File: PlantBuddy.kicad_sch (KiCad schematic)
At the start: 72 parts, among them J1 USB_C_Receptacle_USB2.0, J101 JST, J102 J-Link SWD, J4 External, SW1 SW_Push, U1 LTR-303ALS-01, U101 ME6231C33M5G, U102 nRF52832-QFAA, U104 XB5350A, U105 CN809T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

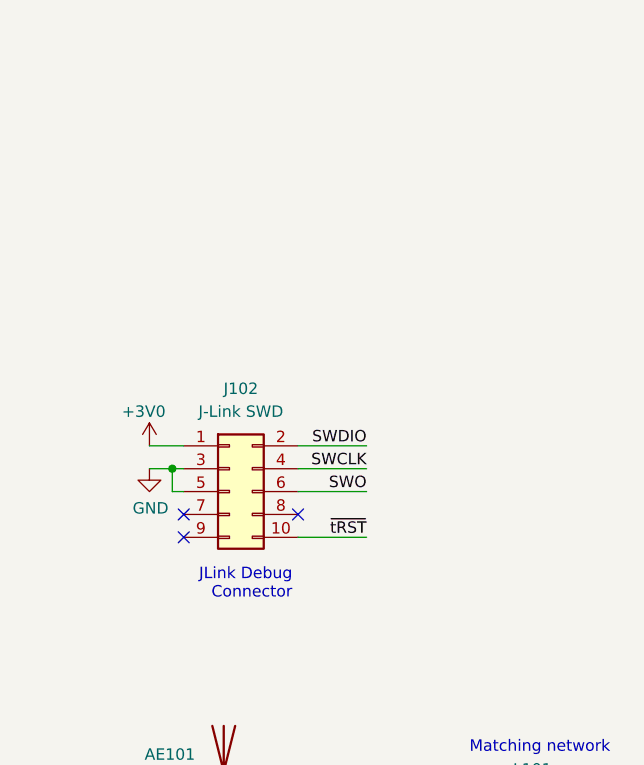
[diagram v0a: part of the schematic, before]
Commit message: Exchanged debug connector for Tag-Connect TC2030-CTX-NL
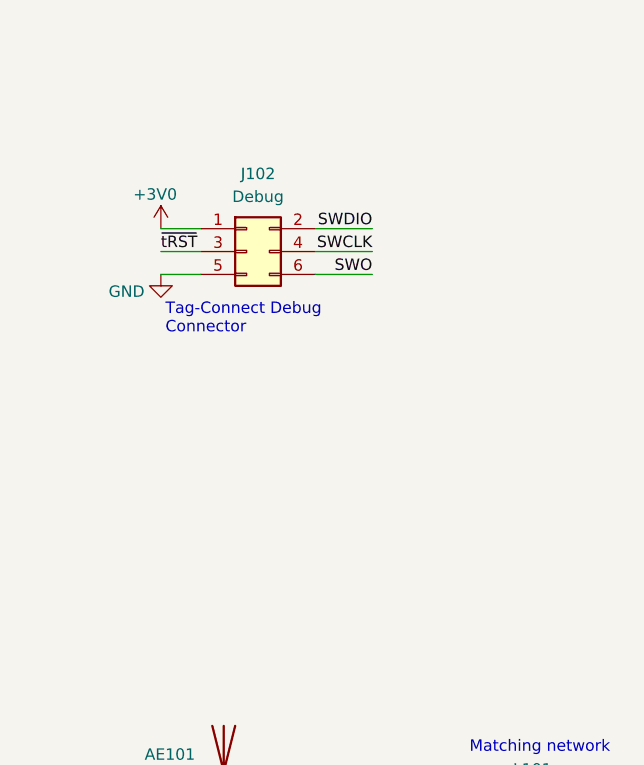
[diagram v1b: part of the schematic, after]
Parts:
- removed J102: J-Link SWD, Connector_PinHeader_1.27mm:PinHeader_2x05_P1.27mm_Vertical, symbol Connector_Generic:Conn_02x05_Odd_Even
- added J102: Debug, Connector:Tag-Connect_TC2030-IDC-NL_2x03_P1.27mm_Vertical, symbol Connector_Generic:Conn_02x03_Odd_Even
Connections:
- net +3V0: now also J102.1 (Pin_1)
- net GND: now also J102.5 (Pin_5)
- net SWCLK: now also J102.4 (Pin_4)
- net SWDIO: now also J102.2 (Pin_2)
- net SWO: now also J102.6 (Pin_6)
- net ~{tRST}: now also J102.3 (Pin_3)
- no-connect marks 26 -> 23
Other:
- note added: "Tag-Connect Debug Connector"
- note removed: "JLink Debug Connector"

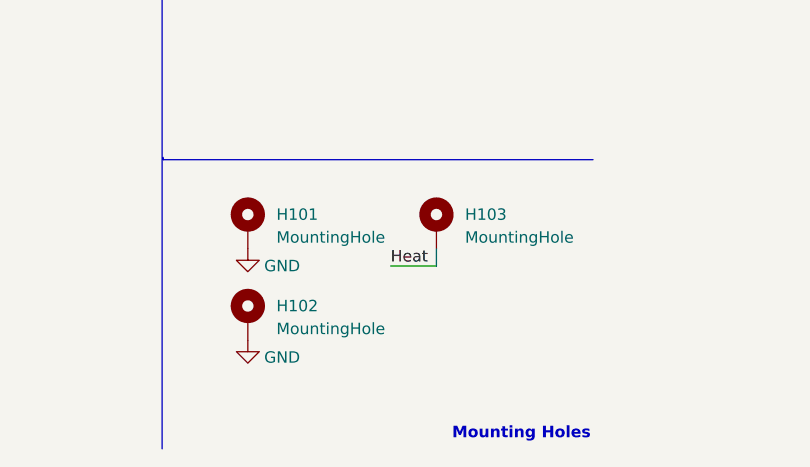
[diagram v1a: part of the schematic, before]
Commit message: Added JLCPCB tooling holes & moved mounting holes.
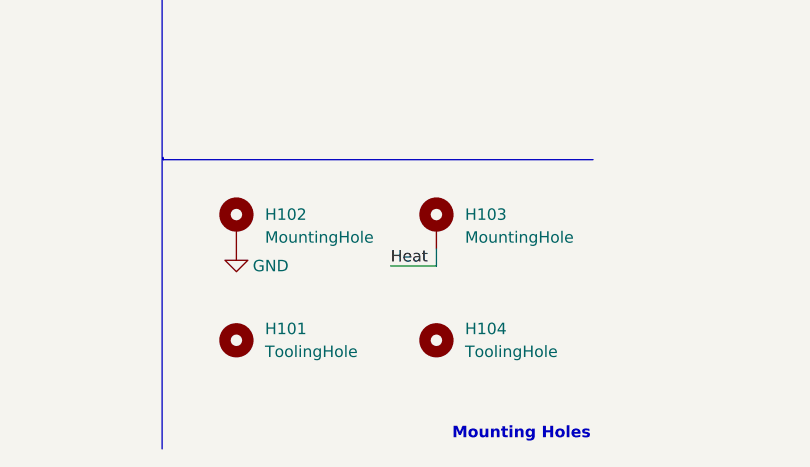
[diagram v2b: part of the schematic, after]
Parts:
- removed H101: MountingHole, MountingHole:MountingHole_2.2mm_M2_DIN965_Pad, symbol Mechanical:MountingHole_Pad
- added H101, H104: ToolingHole, Tooling:JLCPCB_Tooling_hole, symbol Mechanical:MountingHole
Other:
- moved on the sheet: H102
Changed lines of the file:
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@@
     (pin "3")
+  )
+  (symbol (lib_id "Mechanical:MountingHole") (at 282.575 273.05 0) (unit 1)
+    (in_bom yes) (on_board yes) (fields_autoplaced)
+    (property "Reference" "H104" (id 0) (at 285.75 271.7799 0)
+      (effects (font (size 1.27 1.27)) (justify left))
+    )
+    (property "Value" "ToolingHole" (id 1) (at 285.75 274.3199 0)
+      (effects (font (size 1.27 1.27)) (justify left))
+    )
+    (property "Footprint" "Tooling:JLCPCB_Tooling_hole" (id 2) (at 282.575 273.05 0)
+      (effects (font (size 1.27 1.27)) hide)
+    )
+    (property "Datasheet" "~" (id 3) (at 282.575 273.05 0)
+      (effects (font (size 1.27 1.27)) hide)
+    )
   )
   (symbol (lib_id "Connector:TestPoint_Small") (at 397.51 31.75 0) (unit 1)
@@
     (pin "9")
   )
-  (symbol (lib_id "PlantBuddy-rescue:GND-power") (at 261.62 273.05 0) (mirror y) (unit 1)
-    (in_bom yes) (on_board yes)
-    (property "Reference" "#PWR0115" (id 0) (at 261.62 279.4 0)
-      (effects (font (size 1.27 1.27)) hide)
-    )
-    (property "Value" "GND" (id 1) (at 265.43 274.955 0))
-    (property "Footprint" "" (id 2) (at 261.62 273.05 0)
-      (effects (font (size 1.27 1.27)) hide)
-    )
-    (property "Datasheet" "" (id 3) (at 261.62 273.05 0)
+  (symbol (lib_id "PlantBuddy-rescue:GND-power") (at 260.35 262.89 0) (mirror y) (unit 1)
+    (in_bom yes) (on_board yes)
+    (property "Reference" "#PWR0115" (id 0) (at 260.35 269.24 0)
+      (effects (font (size 1.27 1.27)) hide)
+    )
+    (property "Value" "GND" (id 1) (at 264.16 264.795 0))
+    (property "Footprint" "" (id 2) (at 260.35 262.89 0)
+      (effects (font (size 1.27 1.27)) hide)
+    )
+    (property "Datasheet" "" (id 3) (at 260.35 262.89 0)
       (effects (font (size 1.27 1.27)) hide)
     )
@@
     (pin "1")
   )
+  (symbol (lib_id "Mechanical:MountingHole") (at 260.35 273.05 0) (unit 1)
+    (in_bom yes) (on_board yes) (fields_autoplaced)
+    (property "Reference" "H101" (id 0) (at 263.525 271.7799 0)
+      (effects (font (size 1.27 1.27)) (justify left))
+    )
+    (property "Value" "ToolingHole" (id 1) (at 263.525 274.3199 0)
+      (effects (font (size 1.27 1.27)) (justify left))
+    )
+    (property "Footprint" "Tooling:JLCPCB_Tooling_hole" (id 2) (at 260.35 273.05 0)
+      (effects (font (size 1.27 1.27)) hide)
+    )
+    (property "Datasheet" "~" (id 3) (at 260.35 273.05 0)
+      (effects (font (size 1.27 1.27)) hide)
+    )
+  )
   (symbol (lib_id "Device:C_Small") (at 255.27 68.58 0) (unit 1)
     (in_bom yes) (on_board yes) (fields_autoplaced)
@@
     (pin "2")
   )
-  (symbol (lib_id "Mechanical:MountingHole_Pad") (at 261.62 270.51 0) (unit 1)
-    (in_bom yes) (on_board yes) (fields_autoplaced)
-    (property "Reference" "H102" (id 0) (at 264.795 269.2399 0)
-      (effects (font (size 1.27 1.27)) (justify left))
-    )
-    (property "Value" "MountingHole" (id 1) (at 264.795 271.7799 0)
-      (effects (font (size 1.27 1.27)) (justify left))
-    )
-    (property "Footprint" "MountingHole:MountingHole_2.2mm_M2_DIN965_Pad" (id 2) (at 261.62 270.51 0)
-      (effects (font (size 1.27 1.27)) hide)
-    )
-    (property "Datasheet" "~" (id 3) (at 261.62 270.51 0)
+  (symbol (lib_id "Mechanical:MountingHole_Pad") (at 260.35 260.35 0) (unit 1)
+    (in_bom yes) (on_board yes) (fields_autoplaced)
+    (property "Reference" "H102" (id 0) (at 263.525 259.0799 0)
+      (effects (font (size 1.27 1.27)) (justify left))
+    )
+    (property "Value" "MountingHole" (id 1) (at 263.525 261.6199 0)
+      (effects (font (size 1.27 1.27)) (justify left))
+    )
+    (property "Footprint" "MountingHole:MountingHole_2.2mm_M2_DIN965_Pad" (id 2) (at 260.35 260.35 0)
+      (effects (font (size 1.27 1.27)) hide)
+    )
+    (property "Datasheet" "~" (id 3) (at 260.35 260.35 0)
       (effects (font (size 1.27 1.27)) hide)
     )
@@
     (pin "1")
     (pin "2")
-  )
-  (symbol (lib_id "Mechanical:MountingHole_Pad") (at 261.62 260.35 0) (unit 1)
-    (in_bom yes) (on_board yes) (fields_autoplaced)
-    (property "Reference" "H101" (id 0) (at 264.795 259.0799 0)
-      (effects (font (size 1.27 1.27)) (justify left))
-    )
-    (property "Value" "MountingHole" (id 1) (at 264.795 261.6199 0)
-      (effects (font (size 1.27 1.27)) (justify left))
-    )
-    (property "Footprint" "MountingHole:MountingHole_2.2mm_M2_DIN965_Pad" (id 2) (at 261.62 260.35 0)
-      (effects (font (size 1.27 1.27)) hide)
-    )
-    (property "Datasheet" "~" (id 3) (at 261.62 260.35 0)
-      (effects (font (size 1.27 1.27)) hide)
-    )
-    (pin "1")
   )
   (symbol (lib_id "Device:C_Small") (at 42.545 210.185 0) (unit 1)
@@
     )
     (property "Datasheet" "" (id 3) (at 27.305 59.69 0)
-      (effects (font (size 1.27 1.27)) hide)
-    )
-    (pin "1")
-  )
-  (symbol (lib_id "PlantBuddy-rescue:GND-power") (at 261.62 262.89 0) (mirror y) (unit 1)
-    (in_bom yes) (on_board yes)
-    (property "Reference" "#PWR0114" (id 0) (at 261.62 269.24 0)
-      (effects (font (size 1.27 1.27)) hide)
-    )
-    (property "Value" "GND" (id 1) (at 265.43 264.795 0))
-    (property "Footprint" "" (id 2) (at 261.62 262.89 0)
-      (effects (font (size 1.27 1.27)) hide)
-    )
-    (property "Datasheet" "" (id 3) (at 261.62 262.89 0)
       (effects (font (size 1.27 1.27)) hide)
     )
@@
       (reference "#PWR0113") (unit 1) (value "+3V0") (footprint "")
     )
-    (path "/db84b12a-b1cb-4bd2-837a-de0a904c1f94"
-      (reference "#PWR0114") (unit 1) (value "GND") (footprint "")
-    )
     (path "/2d6a005c-7a1d-4c40-b843-d55d362e0b4b"
       (reference "#PWR0115") (unit 1) (value "GND") (footprint "")
@@
       (reference "D102") (unit 1) (value "LED_RGBA") (footprint "LED_SMD:LED_Lumex_SML-LX0404SIUPGUSB")
     )
-    (path "/9dcf973c-88d9-4131-8ddc-a2d315b8f9e4"
-      (reference "H101") (unit 1) (value "MountingHole") (footprint "MountingHole:MountingHole_2.2mm_M2_DIN965_Pad")
+    (path "/8111a967-c093-491f-97fe-4178a7b81b23"
+      (reference "H101") (unit 1) (value "ToolingHole") (footprint "Tooling:JLCPCB_Tooling_hole")
     )
     (path "/8ab94929-ad36-4747-8cd3-d4e063f12079"
@@
       (reference "H103") (unit 1) (value "MountingHole") (footprint "MountingHole:MountingHole_2.2mm_M2_DIN965_Pad")
     )
+    (path "/1b909cb5-2d26-4c06-b8a7-78dae45bfa2b"
+      (reference "H104") (unit 1) (value "ToolingHole") (footprint "Tooling:JLCPCB_Tooling_hole")
+    )
     (path "/4138c96d-aa03-4df3-a048-35a223d1d760"

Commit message: Switched LDO to a better, brand-name one.
- Also am now powering the i2c sensors directly from the LDO because I
noticed current spikes in the previous EN -> measure -> DIS
implementation.
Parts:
- U101, U5: value ME6231C33M5G -> AP2139AK-3.0TRG1; LCSC C610253 -> C3003073
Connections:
- net +3V0: now also C1.1, C2.1, R3.2, R4.2, U1.1 (VDD), U2.1 (VDD)
- net S_3V0: no longer C1.1, C2.1, R3.2, R4.2, U1.1 (VDD), U2.1 (VDD)
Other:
- note removed: "2uA q.current"
- note removed: "600mA LDO"
- moved on the sheet: C1, C2, J4, R3, R4, U1, U2

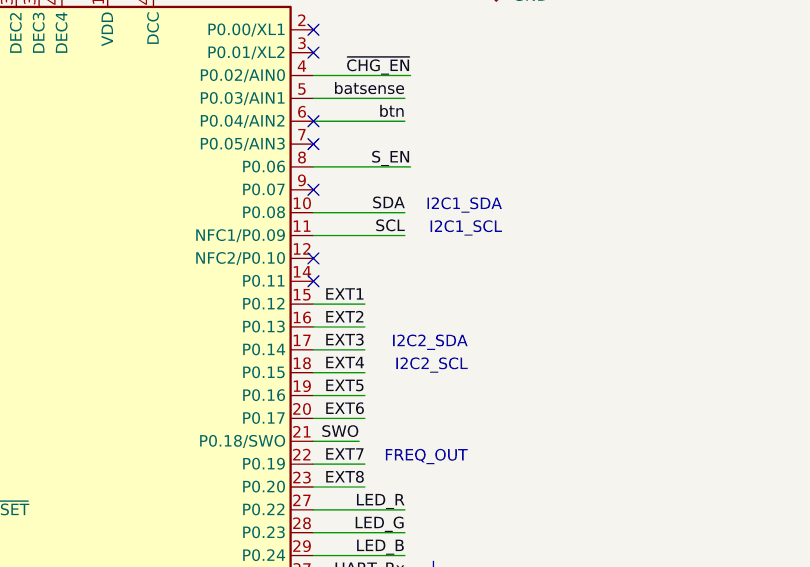
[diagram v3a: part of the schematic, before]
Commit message: Switched to single i2c bus.
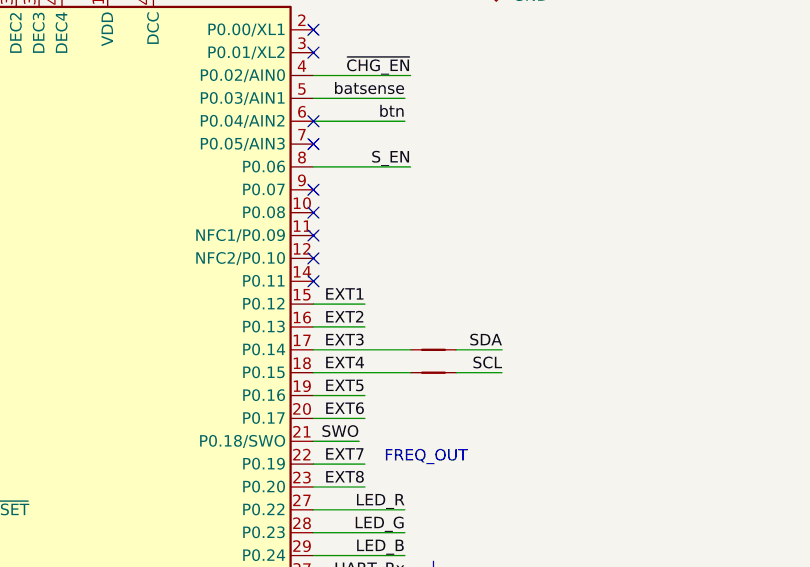
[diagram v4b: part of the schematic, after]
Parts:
- added NT101, NT102: NetTie_2, NetTie:NetTie-2_SMD_Pad0.5mm, symbol Device:NetTie_2
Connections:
- net EXT3: now also NT101.1
- net EXT4: now also NT102.2
- net SCL: now also NT102.1; no longer U102.11 (NFC1/P0.09)
- net SDA: now also NT101.2; no longer U102.10 (P0.08)
- no-connect marks 23 -> 25
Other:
- note removed: "I2C1_SCL"
- note removed: "I2C1_SDA"
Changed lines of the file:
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@@
   (no_connect (at 127.635 160.655))
   (no_connect (at 127.635 163.195))
+  (no_connect (at 127.635 180.975))
+  (no_connect (at 127.635 183.515))
   (no_connect (at 127.635 186.055))
   (no_connect (at 162.56 64.135))
@@
     (stroke (width 0) (type default) (color 0 0 0 0))
   )
+  (wire (pts (xy 127.635 198.755) (xy 138.43 198.755))
+    (stroke (width 0) (type default) (color 0 0 0 0))
+  )
   (wire (pts (xy 147.32 22.225) (xy 147.32 23.495))
     (stroke (width 0) (type default) (color 0 0 0 0))
@@
     (stroke (width 0) (type default) (color 0 0 0 0))
   )
-  (wire (pts (xy 127.635 183.515) (xy 137.795 183.515))
-    (stroke (width 0) (type default) (color 0 0 0 0))
-  )
   (wire (pts (xy 115.57 154.94) (xy 126.365 154.94))
     (stroke (width 0) (type default) (color 0 0 0 0))
@@
     (stroke (width 0) (type default) (color 0 0 0 0))
   )
-  (wire (pts (xy 127.635 180.975) (xy 137.795 180.975))
-    (stroke (width 0) (type default) (color 0 0 0 0))
-  )
   (wire (pts (xy 121.92 125.095) (xy 121.92 126.365))
     (stroke (width 0) (type default) (color 0 0 0 0))
@@
     (stroke (width 0) (type default) (color 0 0 0 0))
   )
-  (wire (pts (xy 133.35 198.755) (xy 127.635 198.755))
-    (stroke (width 0) (type default) (color 0 0 0 0))
-  )
   (wire (pts (xy 104.775 147.32) (xy 115.57 147.32))
     (stroke (width 0) (type default) (color 0 0 0 0))
@@
     (stroke (width 0) (type default) (color 0 0 0 0))
   )
+  (wire (pts (xy 143.51 196.215) (xy 148.59 196.215))
+    (stroke (width 0) (type default) (color 0 0 0 0))
+  )
   (wire (pts (xy 42.545 203.835) (xy 42.545 207.645))
     (stroke (width 0) (type default) (color 0 0 0 0))
@@
     (stroke (width 0) (type default) (color 0 0 0 0))
   )
+  (wire (pts (xy 143.51 198.755) (xy 148.59 198.755))
+    (stroke (width 0) (type default) (color 0 0 0 0))
+  )
   (wire (pts (xy 364.998 34.29) (xy 371.348 34.29))
     (stroke (width 0) (type default) (color 0 0 0 0))
@@
     (stroke (width 0) (type default) (color 0 0 0 0))
   )
-  (wire (pts (xy 133.35 196.215) (xy 127.635 196.215))
+  (wire (pts (xy 291.465 72.39) (xy 300.355 72.39))
     (stroke (width 0) (type default) (color 0 0 0 0))
   )
-  (wire (pts (xy 291.465 72.39) (xy 300.355 72.39))
+  (wire (pts (xy 127.635 196.215) (xy 138.43 196.215))
     (stroke (width 0) (type default) (color 0 0 0 0))
   )
@@
     (effects (font (size 1.27 1.27) bold) (justify right bottom))
   )
-  (text "I2C2_SCL" (at 144.78 198.755 180)
-    (effects (font (size 1.27 1.27)) (justify right bottom))
-  )
   (text "I2C2_SDA" (at 319.278 130.556 0)
     (effects (font (size 1.27 1.27)) (justify left bottom))
   )
-  (text "I2C2_SDA" (at 144.78 196.215 180)
-    (effects (font (size 1.27 1.27)) (justify right bottom))
-  )
   (text "Sensor Power Supply" (at 407.797 97.536 180)
     (effects (font (size 1.27 1.27) bold) (justify right bottom))
@@
     (effects (font (size 1.27 1.27)) (justify right bottom))
   )
-  (text "I2C1_SCL" (at 148.59 183.515 180)
-    (effects (font (size 1.27 1.27)) (justify right bottom))
-  )
   (text "Note: Bind to\nchip's VSS" (at 98.425 138.43 0)
     (effects (font (size 1.27 1.27)) (justify left bottom))
   )
   (text "1) I am using the nRF52832 in DCDC mode and without external LF Oscillator"
-    (at 337.185 171.45 0)
+    (at 337.185 171.45 180)
     (effects (font (size 1.27 1.27)) (justify right bottom))
   )
@@
     (effects (font (size 1 1) italic) (justify left bottom))
   )
-  (text "I2C1_SDA" (at 148.59 180.975 180)
-    (effects (font (size 1.27 1.27)) (justify right bottom))
-  )
   (text "Findings:" (at 256.032 182.626 0)
     (effects (font (size 2.54 2.54) (thickness 0.4) bold) (justify left bottom))
   )
   (text "Regulator gets disabled if nRF52\nis in reset because of the pull-down\nresistor."
-    (at 401.193 92.71 0)
+    (at 401.193 92.71 180)
     (effects (font (size 1.27 1.27)) (justify right bottom))
   )
@@
     (effects (font (size 1.27 1.27)) (justify right bottom))
   )
-  (label "SDA" (at 137.795 180.975 180)
+  (label "SDA" (at 148.59 196.215 180)
     (effects (font (size 1.27 1.27)) (justify right bottom))
   )
@@
     (effects (font (size 1.27 1.27)) (justify right bottom))
   )
-  (label "SCL" (at 137.795 183.515 180)
+  (label "SCL" (at 148.59 198.755 180)
     (effects (font (size 1.27 1.27)) (justify right bottom))
   )
@@
   (symbol (lib_id "power:+3V0") (at 286.385 99.695 0) (unit 1)
     (in_bom yes) (on_board yes)
-    (property "Reference" "#PWR?" (id 0) (at 286.385 103.505 0)
+    (property "Reference" "#PWR0120" (id 0) (at 286.385 103.505 0)
       (effects (font (size 1.27 1.27)) hide)
     )
@@
   (symbol (lib_id "power:+3V0") (at 314.96 99.695 0) (unit 1)
     (in_bom yes) (on_board yes)
-    (property "Reference" "#PWR?" (id 0) (at 314.96 103.505 0)
+    (property "Reference" "#PWR0116" (id 0) (at 314.96 103.505 0)
       (effects (font (size 1.27 1.27)) hide)
     )
@@
     (pin "2")
   )
+  (symbol (lib_id "Device:NetTie_2") (at 140.97 196.215 0) (unit 1)
+    (in_bom yes) (on_board yes) (fields_autoplaced)
+    (property "Reference" "NT101" (id 0) (at 140.97 193.675 0)
+      (effects (font (size 1.27 1.27)) hide)
+    )
+    (property "Value" "NetTie_2" (id 1) (at 140.97 193.675 0)
+      (effects (font (size 1.27 1.27)) hide)
+    )
+    (property "Footprint" "NetTie:NetTie-2_SMD_Pad0.5mm" (id 2) (at 140.97 196.215 0)
+      (effects (font (size 1.27 1.27)) hide)
+    )
+    (property "Datasheet" "~" (id 3) (at 140.97 196.215 0)
+      (effects (font (size 1.27 1.27)) hide)
+    )
+    (pin "1")
+    (pin "2")
+  )
   (symbol (lib_id "Mechanical:MountingHole_Pad") (at 282.575 260.35 0) (unit 1)
     (in_bom yes) (on_board yes) (fields_autoplaced)
@@
   (symbol (lib_id "power:+3V0") (at 286.385 133.35 0) (unit 1)
     (in_bom yes) (on_board yes)
-    (property "Reference" "#PWR?" (id 0) (at 286.385 137.16 0)
+    (property "Reference" "#PWR0114" (id 0) (at 286.385 137.16 0)
       (effects (font (size 1.27 1.27)) hide)
     )
@@
     (pin "1")
   )
+  (symbol (lib_id "Device:NetTie_2") (at 140.97 198.755 0) (mirror y) (unit 1)
+    (in_bom yes) (on_board yes) (fields_autoplaced)
+    (property "Reference" "NT102" (id 0) (at 140.97 196.215 0)
+      (effects (font (size 1.27 1.27)) hide)
+    )
+    (property "Value" "NetTie_2" (id 1) (at 140.97 196.215 0)
+      (effects (font (size 1.27 1.27)) hide)
+    )
+    (property "Footprint" "NetTie:NetTie-2_SMD_Pad0.5mm" (id 2) (at 140.97 198.755 0)
+      (effects (font (size 1.27 1.27)) hide)
+    )
+    (property "Datasheet" "~" (id 3) (at 140.97 198.755 0)
+      (effects (font (size 1.27 1.27)) hide)
+    )
+    (pin "1")
+    (pin "2")
+  )
   (symbol (lib_id "power:VBUS") (at 62.865 45.085 0) (mirror y) (unit 1)
     (in_bom yes) (on_board yes)
@@
       (reference "#PWR0113") (unit 1) (value "+3V0") (footprint "")
     )
+    (path "/f398437c-2539-4f0d-be9b-409c75319c6e"
+      (reference "#PWR0114") (unit 1) (value "+3V0") (footprint "")
+    )
     (path "/2d6a005c-7a1d-4c40-b843-d55d362e0b4b"
       (reference "#PWR0115") (unit 1) (value "GND") (footprint "")
     )
+    (path "/b2fe01b5-922b-4b48-a54c-2df20434d6ac"
+      (reference "#PWR0116") (unit 1) (value "+3V0") (footprint "")
+    )
     (path "/263f1c26-8251-455e-97bd-1a3c3f0aebfc"
       (reference "#PWR0117") (unit 1) (value "GND") (footprint "")
@@
       (reference "#PWR0119") (unit 1) (value "GND") (footprint "")
     )
+    (path "/a2fd2841-6e64-4279-8d4b-d012b9e56928"
+      (reference "#PWR0120") (unit 1) (value "+3V0") (footprint "")
+    )
     (path "/36f1eb4a-d699-4504-a771-be3e978b3a9a"
       (reference "#PWR0122") (unit 1) (value "GND") (footprint "")
@@
       (reference "#PWR0135") (unit 1) (value "GND") (footprint "")
     )
-    (path "/a2fd2841-6e64-4279-8d4b-d012b9e56928"
-      (reference "#PWR?") (unit 1) (value "+3V0") (footprint "")
-    )
-    (path "/b2fe01b5-922b-4b48-a54c-2df20434d6ac"
-      (reference "#PWR?") (unit 1) (value "+3V0") (footprint "")
-    )
-    (path "/f398437c-2539-4f0d-be9b-409c75319c6e"
-      (reference "#PWR?") (unit 1) (value "+3V0") (footprint "")
-    )
     (path "/400ec827-23d4-4dc8-9011-0b8d912989c5"
       (reference "AE101") (unit 1) (value "Antenna_Chip") (footprint "LED_SMD:LED_1206_3216Metric")
@@
       (reference "L103") (unit 1) (value "15nH") (footprint "Inductor_SMD:L_0402_1005Metric")
     )
+    (path "/d1fb8675-3cf7-4997-a579-700b7a9b6bd4"
+      (reference "NT101") (unit 1) (value "NetTie_2") (footprint "NetTie:NetTie-2_SMD_Pad0.5mm")
+    )
+    (path "/f9fc0c57-1b6c-486e-a214-face085f8bdd"
+      (reference "NT102") (unit 1) (value "NetTie_2") (footprint "NetTie:NetTie-2_SMD_Pad0.5mm")
+    )
     (path "/1ee7e9b3-fe66-4649-82e6-ac5fe79d7949"
